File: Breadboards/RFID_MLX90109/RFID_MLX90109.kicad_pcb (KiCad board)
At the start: 2 copper layers, 50.8 x 37.6 mm, 24 parts, among them P101 CONN_01X08, Q101 Q_NMOS_GSD, U101 MLX90109

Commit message: Adds 125kHz antenna to Layout
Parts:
- added AE108: Antenna_Loop, Octanis3:125kHz_PCB_Antenna, B.Cu at (132.8, 63.1)
- added AE109: Antenna_Loop, Octanis3:125kHz_PCB_Antenna, F.Cu at (184.2, 63.2)
- added JP102: Jumper_NO_Small, Pin_Headers:Pin_Header_Straight_1x02_Pitch2.54mm, F.Cu at (167.1, 90.9)
- added JP103: Jumper_NO_Small, Pin_Headers:Pin_Header_Straight_1x02_Pitch2.54mm, F.Cu at (149.9, 90.9)
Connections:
- net Net-(AE101-Pad1) renamed /RFID_ANT
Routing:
- net /RFID_ANT: track 59.5 -> 64.8 mm
- net /RFID_VDD: track 111.5 -> 116.8 mm
- net Net-(AE108-Pad2): track 0.00 -> 0.65 mm, vias 0 -> 1
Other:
- board size 50.8 x 37.6 mm -> 52.8 x 95.5 mm

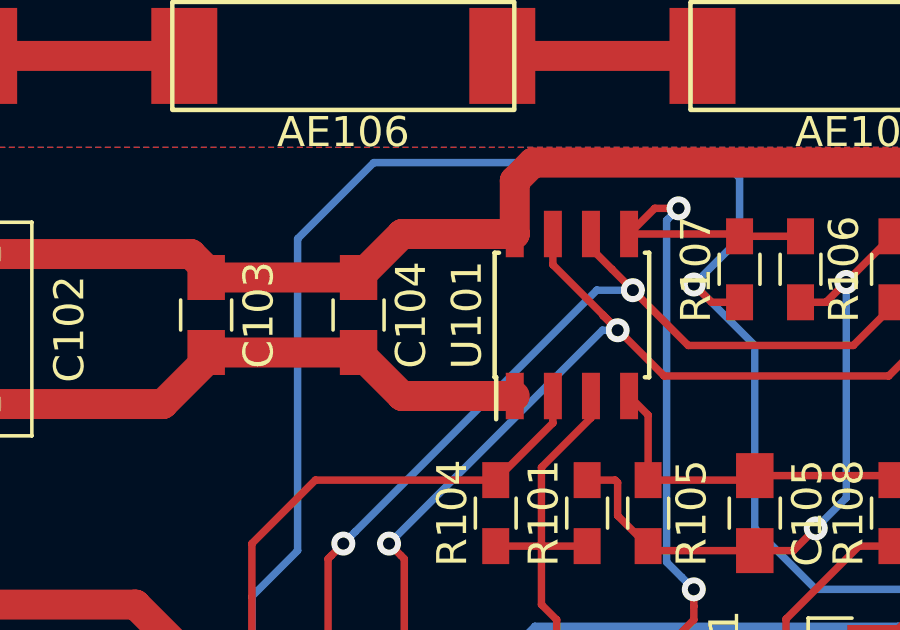
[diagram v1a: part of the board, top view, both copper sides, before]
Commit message: Adds 4 vias for MLX GND connection
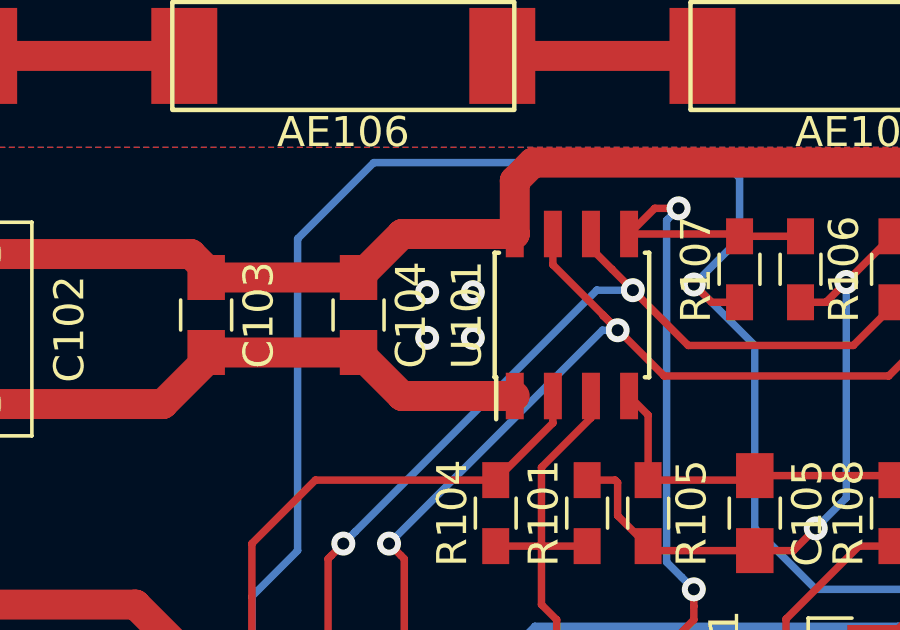
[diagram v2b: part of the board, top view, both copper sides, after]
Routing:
- net GND: vias 2 -> 6
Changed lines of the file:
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@@
     (thickness 1.6)
     (drawings 5)
-    (tracks 162)
+    (tracks 166)
     (zones 0)
     (modules 28)
@@
   )
   (setup
-    (last_trace_width 1)
+    (last_trace_width 0.25)
     (user_trace_width 1)
     (trace_clearance 0.2)
@@
   (gr_line (start 132.08 35.56) (end 184.912 35.56) (layer Edge.Cuts) (width 0.15))
   (gr_line (start 132.08 131.064) (end 132.08 35.56) (layer Edge.Cuts) (width 0.15))
+  (via (at 162.814 117.094) (size 0.8) (drill 0.4) (layers F.Cu B.Cu) (net 2))
+  (via (at 162.814 115.57) (size 0.8) (drill 0.4) (layers F.Cu B.Cu) (net 2))
+  (via (at 161.29 115.57) (size 0.8) (drill 0.4) (layers F.Cu B.Cu) (net 2))
+  (via (at 161.29 117.094) (size 0.8) (drill 0.4) (layers F.Cu B.Cu) (net 2))
   (segment (start 171.196 96.52) (end 170.18 96.52) (width 1) (layer F.Cu) (net 4))
   (segment (start 170.18 96.52) (end 167.132 93.472) (width 1) (layer F.Cu) (net 4))

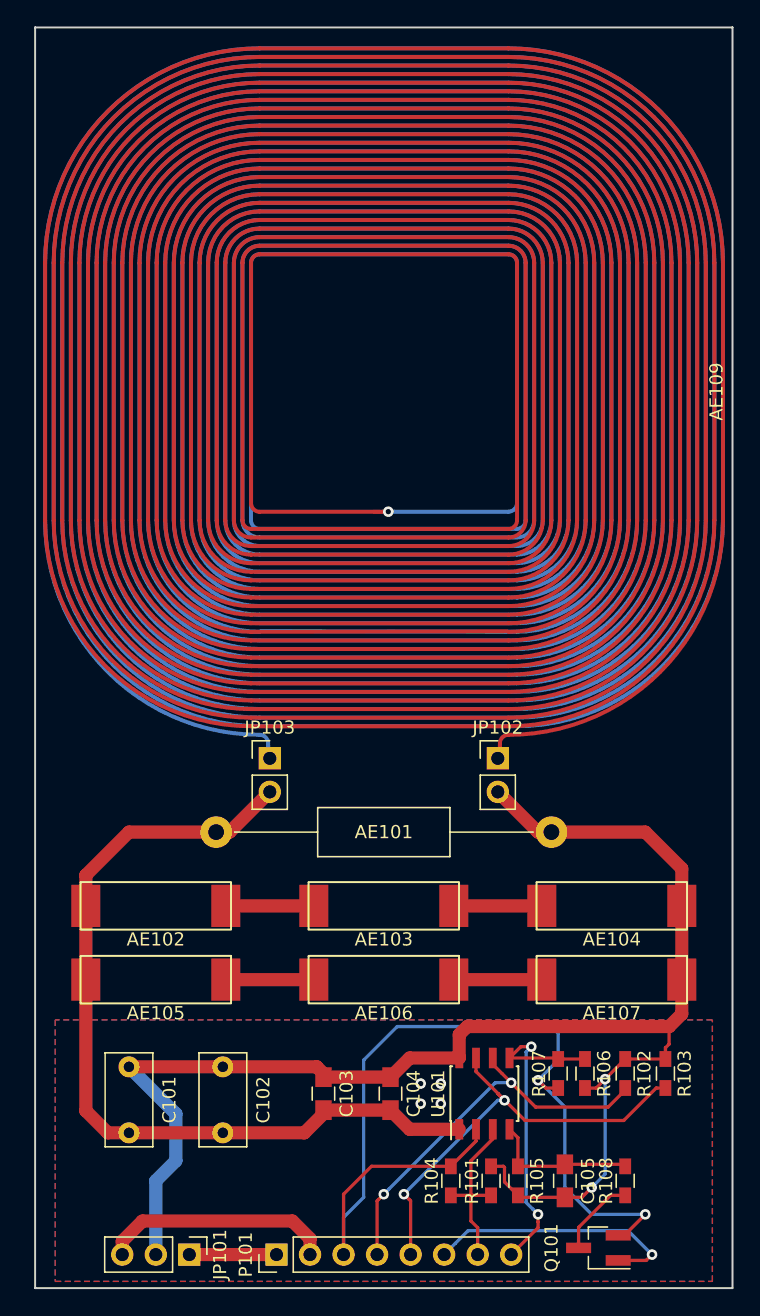
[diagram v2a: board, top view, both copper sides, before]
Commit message: Adds Octanis Logos and Nestbox Logo to layout
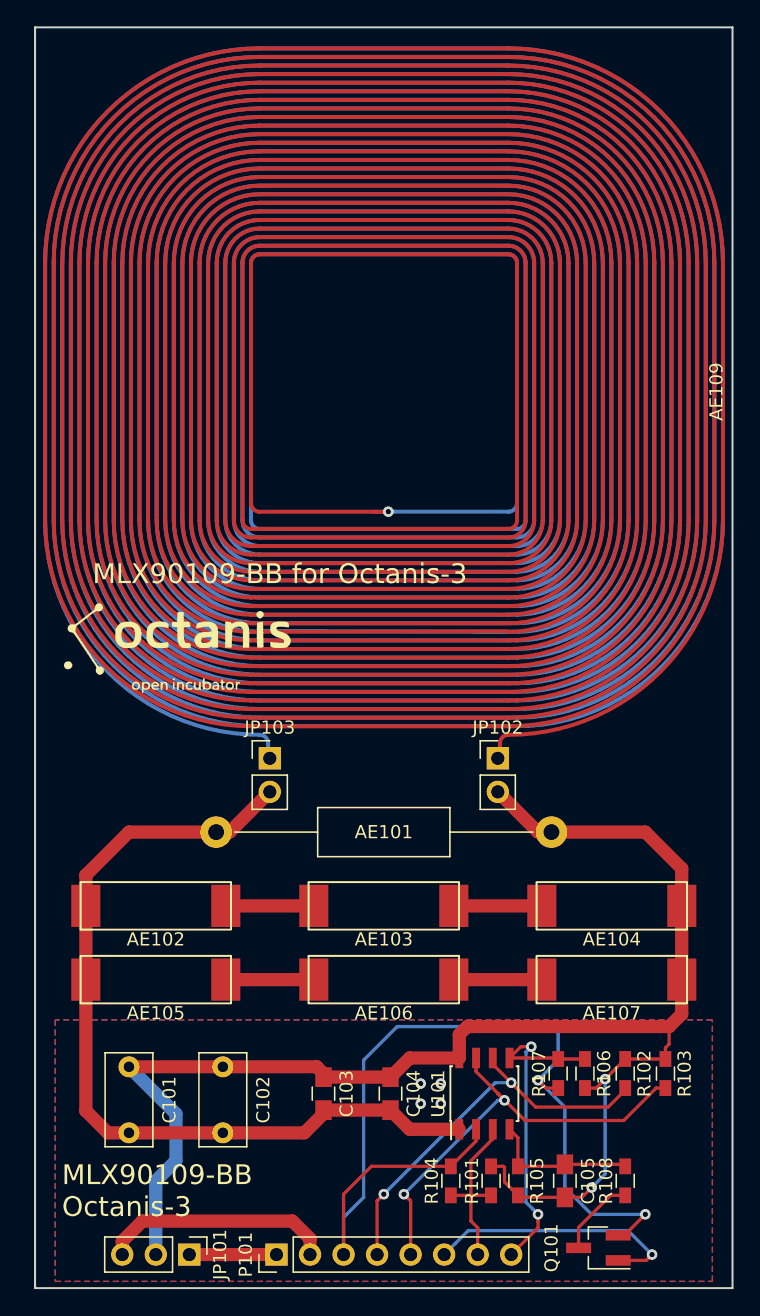
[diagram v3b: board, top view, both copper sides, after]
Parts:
- added G***: LOGO, Octanis3:octanis_open_incubator_logo, F.Cu at (143.0, 82.5)
- added G***: LOGO, Octanis3:octanis3_logo, B.Cu at (153.9, 117.9)
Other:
- board text added: "MLX90109-BB Octanis-3"
- board text added: "MLX90109-BB for Octanis-3"
